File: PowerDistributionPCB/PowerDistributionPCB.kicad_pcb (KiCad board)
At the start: 4 copper layers, 89.8 x 107.2 mm, 68 parts, among them J1 USB3_A, K1 RT314F05(gen), K2 RT314F05(gen), K3 RT314F05(gen), K4 RT314F05(gen), Q1 AOD4185, Q10 MMBT2222A, Q11 MMBT2222A, Q12 MMBT2222A, Q2 MMBT2222A, Q6 MMBT2222A, Q7 MMBT2222A, Q8 MMBT2222A, Q9 MMBT2222A, U1 AP63203WU

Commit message: power traces, cleanup
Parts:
- added G***: LOGO, LOGO, F.Cu at (142.5, 62.4)
- renumbered 12V1 to 12V, 12V_OUT1 to 12V_OUT, 3.3V_OUT1 to 3.3V_OUT, 5V1 to 5V, 5V_OUT1 to 5V_OUT, 22V_BATT_IN1 to BATT_IN, J1 to VN_OUT
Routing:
- net 3.3VBuck: track 31.0 -> 212.9 mm, vias 0 -> 1
- net 5VBuck: track 25.2 -> 179.1 mm
- net 12VBuck: track 18.0 -> 128.0 mm
- net Net-(K4-Pad12.1): track 0.00 -> 7.62 mm
- net Net-(K3-Pad12.1): track 0.00 -> 7.62 mm
- net Net-(K2-Pad12.1): track 0.00 -> 7.62 mm
- net Net-(K1-Pad12.1): track 0.00 -> 7.62 mm
- net VNRelayOut: track 14.3 -> 17.2 mm
- net Sys_Vin: track 88.2 -> 86.3 mm
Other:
- board text added: "3.3V"
- board text added: "ARDUINO"
- board text added: "Power PCB SP26 Jonah Conolly Liya Mei"

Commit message: final updates to schematic and layout connections
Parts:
- added C5: 470u, Capacitor_SMD:CP_Elec_8x10.5, F.Cu at (109.5, 77.0)
- added D9: SS14, Diode_SMD:D_SMA, F.Cu at (120.5, 79.0)
- moved Cout1 4.80 mm to (98.2, 69.4)
- moved Cout2 4.80 mm to (98.2, 66.9)
- moved Cout3 4.80 mm to (98.2, 64.4)
- moved Cout4 4.80 mm to (118.4, 64.9)
- moved C2b1 4.80 mm to (100.7, 59.8)
- moved G*** 4.80 mm to (142.1, 57.6)
- moved Rfbt2 4.80 mm to (95.2, 60.4)
- moved 12V1 4.80 mm to (98.3, 60.4)
- moved C1 4.80 mm to (82.0, 60.8)
- moved C2 4.80 mm to (82.0, 66.7)
- moved Cout5 4.80 mm to (118.4, 67.4)
- moved R3a1 4.80 mm to (82.6, 57.9)
- moved R3b1 4.80 mm to (78.6, 57.9)
- moved Rfbt1 4.80 mm to (115.2, 60.9)
- moved Rmode1a1 4.80 mm to (118.5, 58.4)
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- renumbered 12V to 12V1, 12V_OUT to 12V_OUT1, BATT_IN to 22V_BATT_IN1, 3.3V_OUT to 3.3V_OUT1, 5V to 5V1, 5V_OUT to 5V_OUT1, VN_OUT to J1
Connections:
- A1 pad 27: 5VSafe -> Net-(A1-+5V)
- A1 pad 30: 12VBuck -> unconnected-(A1-VIN-Pad30)
- D10 pad 1: 5VSafe -> 5VBuck
- D2 pad 1: 5VSafe -> 5VBuck
- D3 pad 1: 5VSafe -> 5VBuck
- D4 pad 1: 5VSafe -> 5VBuck
- D5 pad 1: 5VSafe -> 5VBuck
- D6 pad 1: 5VSafe -> 5VBuck
- D7 pad 1: 5VSafe -> 5VBuck
- D8 pad 1: 5VSafe -> 5VBuck
- K1 pad 11.1: 5VBuck -> Net-(K1-Pad11.1)
- K1 pad 11.2: 5VBuck -> Net-(K1-Pad11.1)
- K1 pad 12.1: Net-(K1-Pad12.1) -> 5VBuck
- K1 pad 12.2: Net-(K1-Pad12.1) -> 5VBuck
- K1 pad A3: 5VSafe -> 5VBuck
- K2 pad 11.1: 3.3VBuck -> Net-(K2-Pad11.1)
- K2 pad 11.2: 3.3VBuck -> Net-(K2-Pad11.1)
- K2 pad 12.1: Net-(K2-Pad12.1) -> 3.3VBuck
- K2 pad 12.2: Net-(K2-Pad12.1) -> 3.3VBuck
- K2 pad A3: 5VSafe -> 5VBuck
- K3 pad 11.1: 5VBuck -> Net-(K3-Pad11.1)
- K3 pad 11.2: 5VBuck -> Net-(K3-Pad11.1)
- K3 pad 12.1: Net-(K3-Pad12.1) -> 5VBuck
- K3 pad 12.2: Net-(K3-Pad12.1) -> 5VBuck
- K3 pad A3: 5VSafe -> 5VBuck
- K4 pad 11.1: 12VBuck -> Net-(K4-Pad11.1)
- K4 pad 11.2: 12VBuck -> Net-(K4-Pad11.1)
- K4 pad 12.1: Net-(K4-Pad12.1) -> 12VBuck
- K4 pad 12.2: Net-(K4-Pad12.1) -> 12VBuck
- K4 pad A3: 5VSafe -> 5VBuck
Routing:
- net 5VSafe: track 191.7 -> 0.00 mm
- net 5VBuck: track 179.1 -> 312.5 mm, vias 0 -> 2
- net 3.3VBuck: track 212.9 -> 192.4 mm, vias 1 -> 0
- net Net-(A1-+5V): track 0.00 -> 13.3 mm
- net 12VBuck: track 128.0 -> 119.4 mm, vias 0 -> 1
- net Net-(K4-Pad12.1): track 7.62 -> 0.00 mm
- net Net-(K4-Pad11.1): track 0.00 -> 7.62 mm
- net Net-(K3-Pad12.1): track 7.62 -> 0.00 mm
- net Net-(K3-Pad11.1): track 0.00 -> 7.62 mm
- net Net-(K2-Pad12.1): track 7.62 -> 0.00 mm
- net Net-(K2-Pad11.1): track 0.00 -> 7.62 mm
- net Net-(K1-Pad12.1): track 7.62 -> 0.00 mm
- net Net-(K1-Pad11.1): track 0.00 -> 7.62 mm
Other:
- board size 89.8 x 107.2 mm -> 89.8 x 111.7 mm

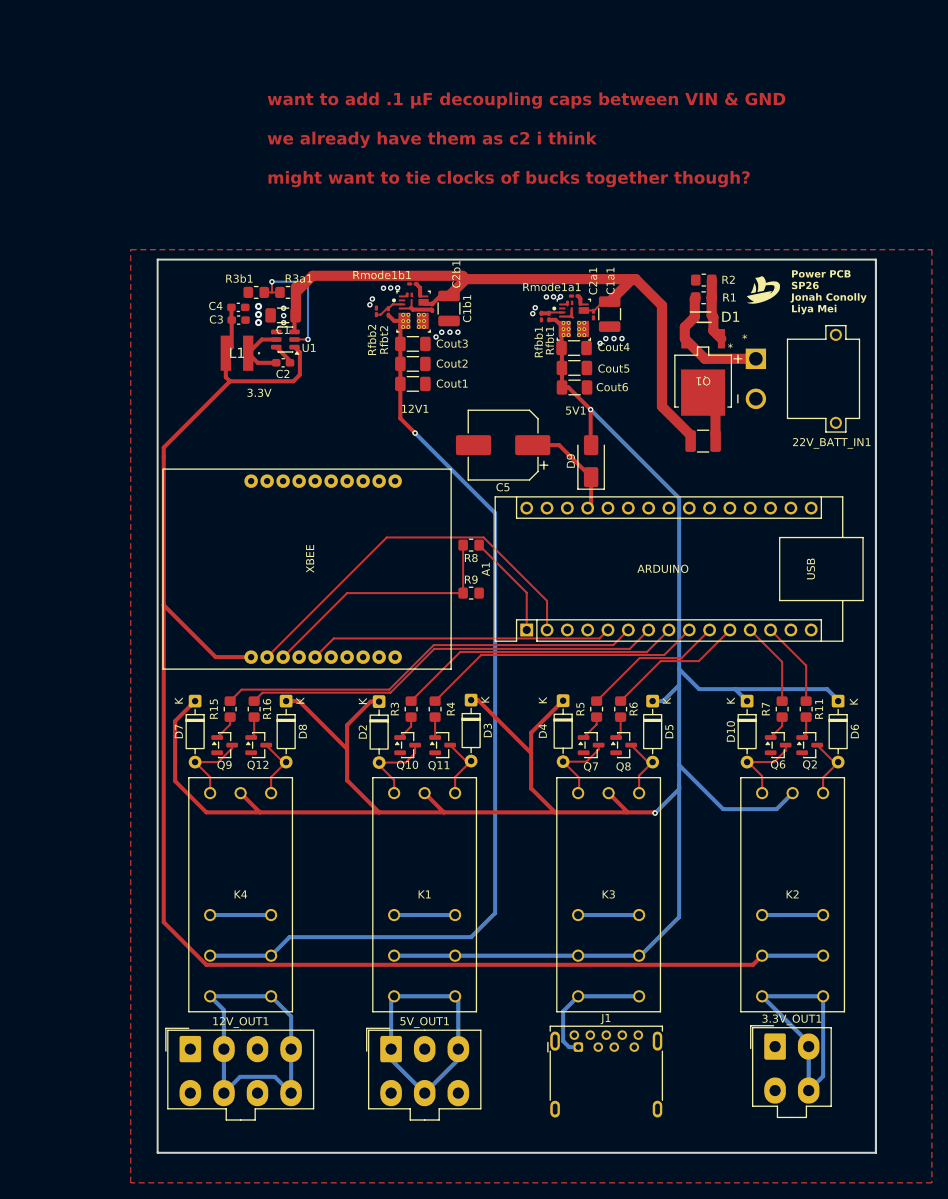
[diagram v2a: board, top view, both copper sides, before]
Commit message: updated battery protection capacitor
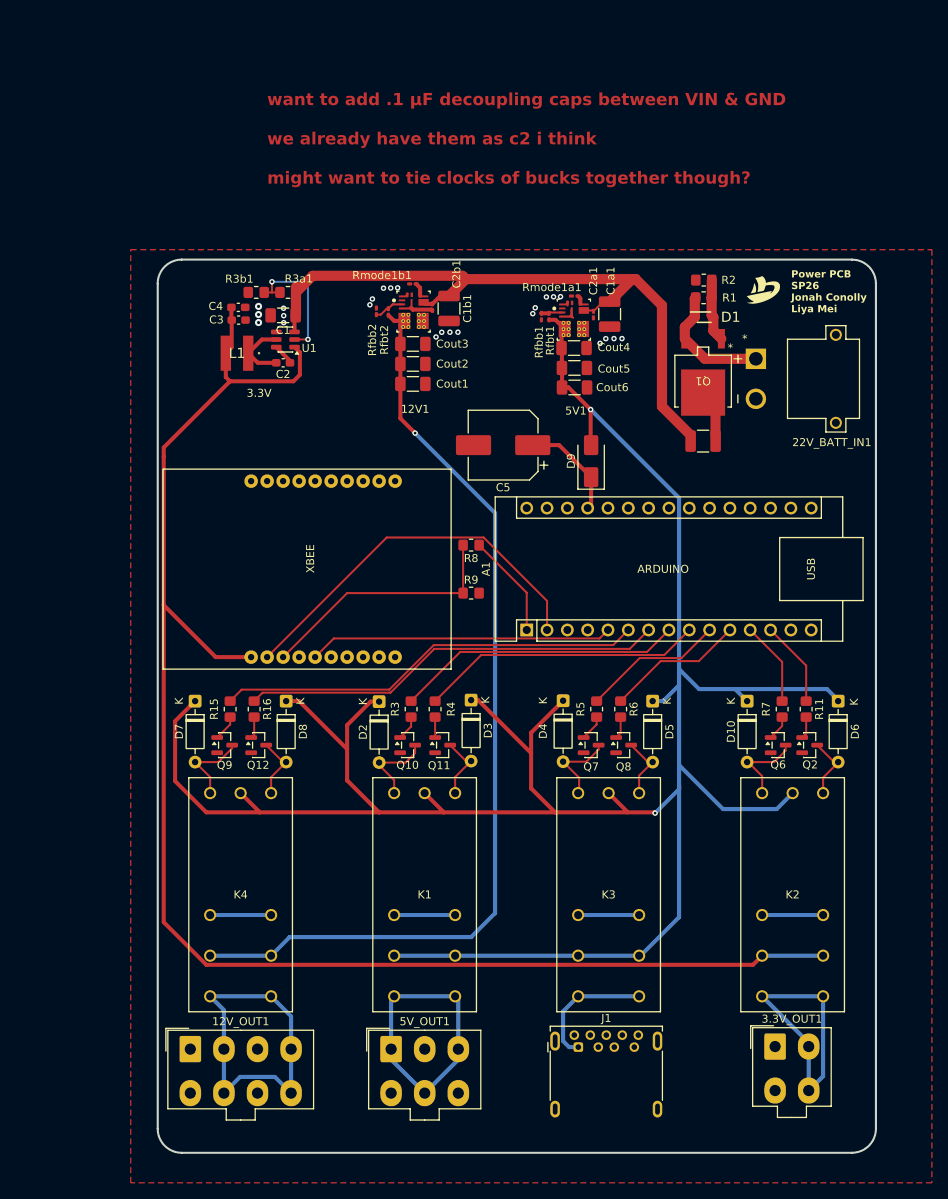
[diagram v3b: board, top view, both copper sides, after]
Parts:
- Main_Bulk(electrolytic)1: value 250µF -> 100µF
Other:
- outline, holes or cut-outs redrawn
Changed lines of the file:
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@@
 			)
 		)
-		(property "Value" "250µF"
+		(property "Value" "100µF"
 			(at 0 2.3 0)
 			(layer "F.Fab")
@@
 		)
 	)
-	(gr_rect
-		(start 66.32 53.81)
-		(end 156.1 165.46)
+	(gr_line
+		(start 153.1 165.46)
+		(end 69.32 165.46)
 		(stroke
 			(width 0.254)
-			(type solid)
+			(type default)
+		)
+		(layer "Edge.Cuts")
+	)
+	(gr_arc
+		(start 69.32 165.46)
+		(mid 67.19868 164.58132)
+		(end 66.32 162.46)
+		(stroke
+			(width 0.254)
+			(type default)
+		)
+		(layer "Edge.Cuts")
+	)
+	(gr_line
+		(start 156.1 56.81)
+		(end 156.1 162.46)
+		(stroke
+			(width 0.254)
+			(type default)
+		)
+		(layer "Edge.Cuts")
+	)
+	(gr_arc
+		(start 156.1 162.46)
+		(mid 155.22132 164.58132)
+		(end 153.1 165.46)
+		(stroke
+			(width 0.254)
+			(type default)
+		)
+		(layer "Edge.Cuts")
+	)
+	(gr_line
+		(start 69.32 53.81)
+		(end 153.1 53.81)
+		(stroke
+			(width 0.254)
+			(type default)
+		)
+		(layer "Edge.Cuts")
+	)
+	(gr_arc
+		(start 153.1 53.81)
+		(mid 155.22132 54.68868)
+		(end 156.1 56.81)
+		(stroke
+			(width 0.254)
+			(type default)
+		)
+		(layer "Edge.Cuts")
+	)
+	(gr_line
+		(start 66.32 162.46)
+		(end 66.32 56.81)
+		(stroke
+			(width 0.254)
+			(type default)
+		)
+		(layer "Edge.Cuts")
+	)
+	(gr_arc
+		(start 66.32 56.81)
+		(mid 67.19868 54.68868)
+		(end 69.32 53.81)
+		(stroke
+			(width 0.254)
+			(type default)
 		)
-		(fill no)
 		(layer "Edge.Cuts")
 	)

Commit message: fixed DRC errors
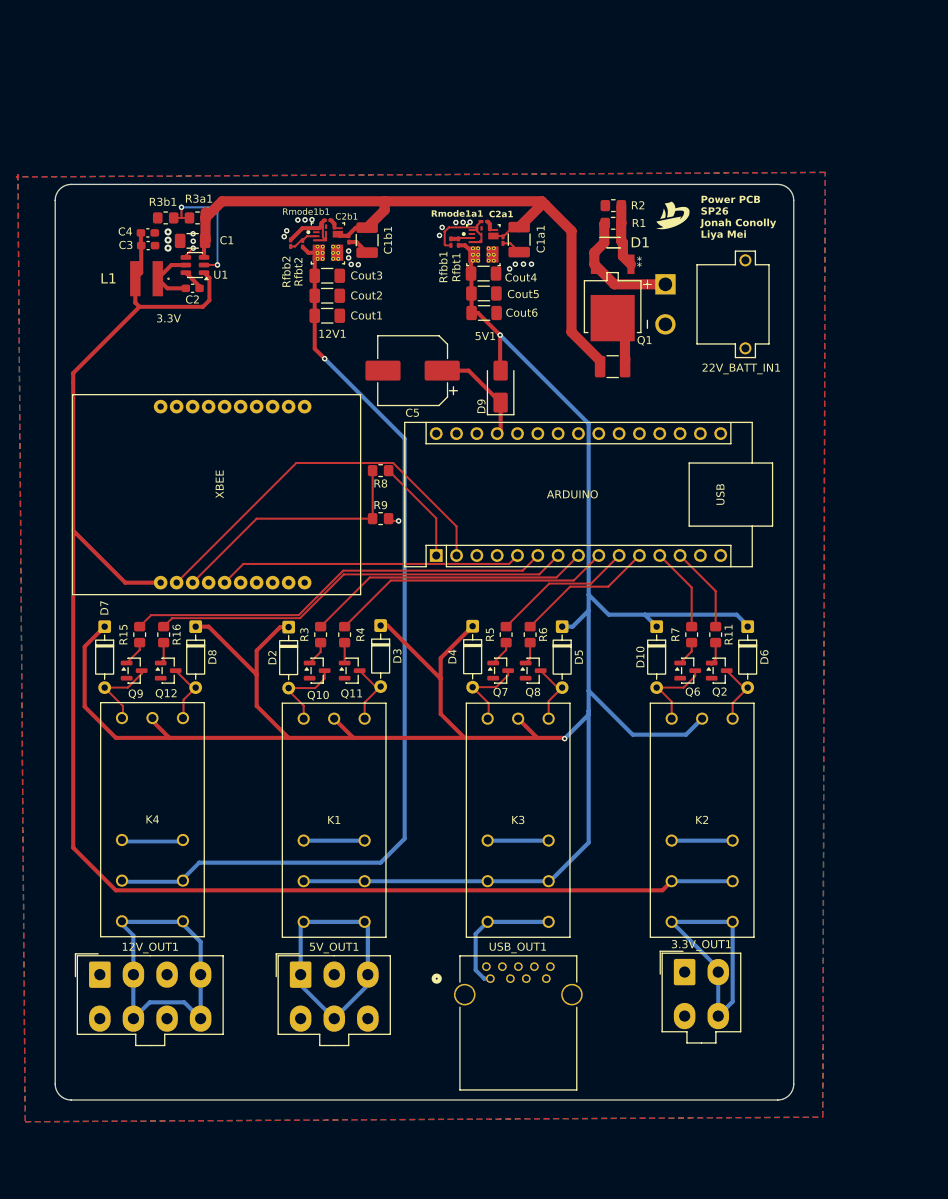
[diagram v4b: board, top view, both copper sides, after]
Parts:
- removed J1: USB3_A, Connector_USB:USB3_A_Molex_48393-001
- added USB_OUT1: 484050003, CUSail:CONN_484050003_MOL, F.Cu at (107.9, 143.7)
- moved R2 14.6 mm to (123.3, 47.1)
- moved 12V_OUT1 14.6 mm to (59.1, 143.2)
- moved 22V_BATT_IN1 14.6 mm to (139.8, 59.4)
- moved 3.3V_OUT1 14.6 mm to (132.2, 142.9)
- moved 5V1 14.6 mm to (107.0, 52.1)
- moved 5V_OUT1 14.6 mm to (84.2, 143.2)
- moved A1 14.6 mm to (101.1, 90.8)
- moved C2a1 14.6 mm to (109.5, 51.4)
- moved C3 14.6 mm to (65.1, 52.1)
- moved C4 14.6 mm to (65.1, 50.5)
- moved C5 14.6 mm to (98.2, 67.7)
- moved Cout6 14.6 mm to (107.1, 60.5)
- moved D10 14.6 mm to (128.7, 99.7)
- moved D2 14.6 mm to (82.7, 99.8)
- moved D3 14.6 mm to (94.2, 99.6)
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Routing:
- net GND: track 5.63 -> 42.3 mm, vias 6 -> 7
- net Sys_Vin: track 86.3 -> 87.5 mm
- net 12VBuck: track 119.4 -> 118.4 mm
- net Net-(12V1-MODE): track 1.70 -> 1.18 mm
- added copper zone on B.Cu, net GND
- added copper zone on In1.Cu, net GND
- added copper zone on In2.Cu, net GND
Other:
- board size 89.8 x 111.7 mm -> 92.3 x 114.5 mm
- board text removed: "want to add .1 µF decoupling caps between VIN & GND we already have them as c2 i think might want to tie clocks of bucks together though?"

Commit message: added clipart
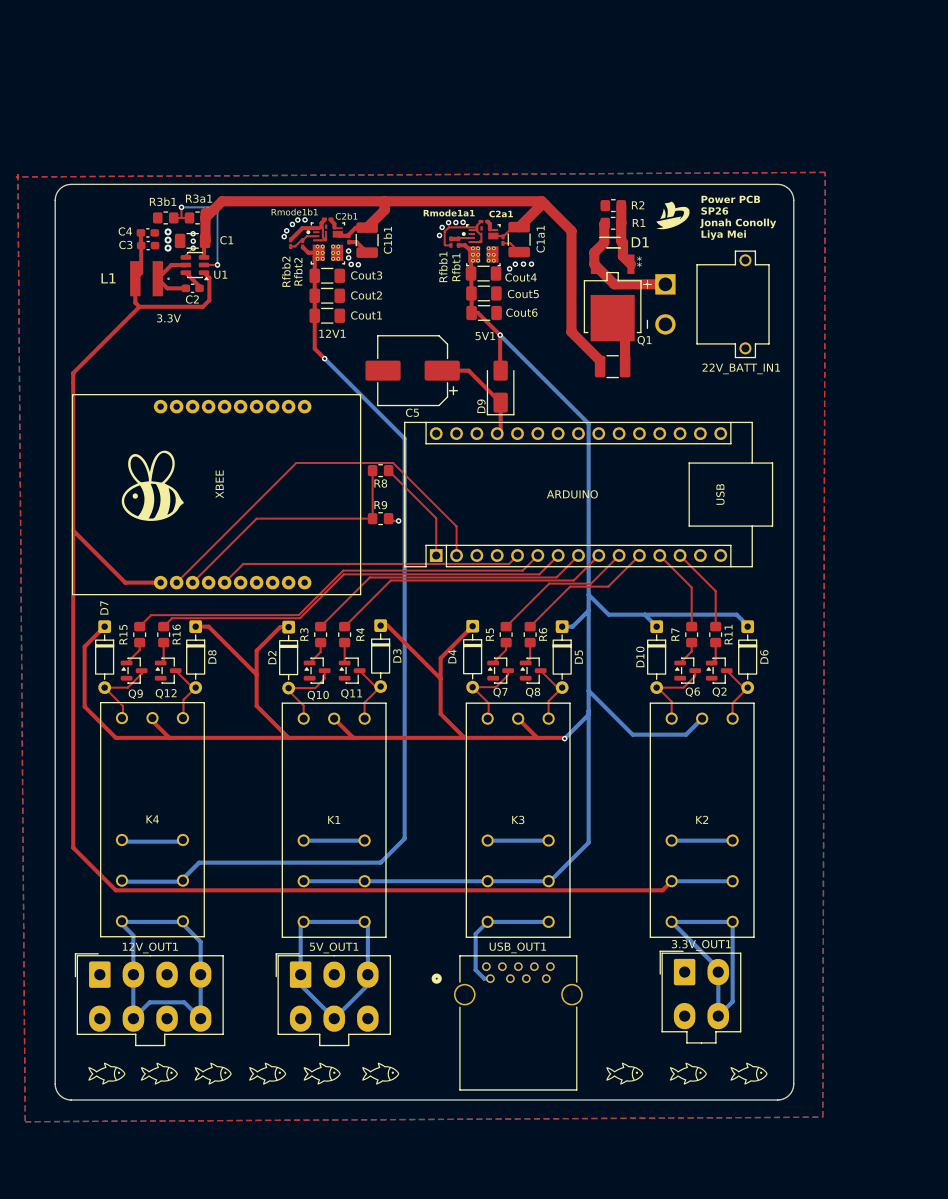
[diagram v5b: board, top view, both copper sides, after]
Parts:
- added G***: LOGO, LOGO, F.Cu at (124.7, 155.6)
- added G***: LOGO, LOGO, F.Cu at (66.5, 155.6)
- added G***: LOGO, LOGO, F.Cu at (132.7, 155.6)
- added G***: LOGO, LOGO, F.Cu at (60.0, 155.6)
- added G***: LOGO, LOGO, F.Cu at (65.8, 82.2)
- added G***: LOGO, LOGO, F.Cu at (94.2, 155.6)
- added G***: LOGO, LOGO, F.Cu at (86.9, 155.6)
- added G***: LOGO, LOGO, F.Cu at (80.1, 155.6)
- added G***: LOGO, LOGO, F.Cu at (140.2, 155.6)
- added G***: LOGO, LOGO, F.Cu at (73.3, 155.6)
- moved Rmode1b1 0.15 mm to (87.6, 48.8)
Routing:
- net GND: track 42.3 -> 41.6 mm

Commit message: new buck stuff
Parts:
- removed C1a1: 10uF, Capacitor_SMD:C_1210_3225Metric_Pad1.33x2.70mm_HandSolder
- removed C2a1: 100nF, Capacitor_SMD:C_0201_0603Metric_Pad0.64x0.40mm_HandSolder
- removed Cout4, Cout5, Cout6: 22uF, Capacitor_SMD:C_1206_3216Metric_Pad1.33x1.80mm_HandSolder
- added Cboot1: 100nF, Capacitor_SMD:C_0201_0603Metric_Pad0.64x0.40mm_HandSolder, F.Cu at (95.4, 45.1)
- added Cff1: 150pF, Capacitor_SMD:C_0201_0603Metric_Pad0.64x0.40mm_HandSolder, F.Cu at (94.0, 52.5)
- added Cin1: 10µF, Capacitor_SMD:C_1210_3225Metric_Pad1.33x2.70mm_HandSolder, F.Cu at (82.4, 46.9)
- added Cin2: 10µF, Capacitor_SMD:C_1210_3225Metric_Pad1.33x2.70mm_HandSolder, F.Cu at (86.4, 46.9)
- added Cinx1: 100nF, Capacitor_SMD:C_0805_2012Metric_Pad1.18x1.45mm_HandSolder, F.Cu at (89.9, 47.0)
- added Cout1a1: 22µF, Capacitor_SMD:C_1210_3225Metric_Pad1.33x2.70mm_HandSolder, F.Cu at (106.9, 48.9)
- added Cout2a1: 22µF, Capacitor_SMD:C_1210_3225Metric_Pad1.33x2.70mm_HandSolder, F.Cu at (110.9, 48.9)
- added Css1: 22nF, Capacitor_SMD:C_0402_1005Metric_Pad0.74x0.62mm_HandSolder, F.Cu at (97.9, 51.4)
- added L1a1: 3.3µH, Inductor_SMD:L_Coilcraft_XAL7070-XXX, F.Cu at (100.5, 45.0)
- added Rpg1: 100kΩ, Resistor_SMD:R_0402_1005Metric_Pad0.72x0.64mm_HandSolder, F.Cu at (96.4, 51.1)
- 5V1: value TPSM84338RCJR -> TPS56A37RPAR; footprint CUSail:buck_correct -> CUSail:TPS56A37RPAR
- Rfbb1: value 10k -> 10kΩ
- Rfbt1: value 73.2k -> 73.2kΩ; footprint Resistor_SMD:R_0201_0603Metric_Pad0.64x0.40mm_HandSolder -> Resistor_SMD:R_0805_2012Metric_Pad1.20x1.40mm_HandSolder
- Rmode1a1: value 18k -> 52.3kΩ; footprint Capacitor_SMD:C_0201_0603Metric_Pad0.64x0.40mm_HandSolder -> Resistor_SMD:R_0402_1005Metric_Pad0.72x0.64mm_HandSolder
- moved Rmode1a1 15.4 mm to (91.9, 51.4), turned to -90 degrees
- moved 5V1 13.6 mm to (94.1, 47.9), turned to 90 degrees
- moved C1b1 13.1 mm to (81.0, 57.5)
- moved Cout1b1 13.1 mm to (76.0, 67.0)
- moved Cout2b1 13.1 mm to (76.0, 64.5)
- moved Cout3b1 13.1 mm to (76.0, 62.0)
- moved Rfbt2 13.1 mm to (72.9, 58.0)
- moved Rmode1b1 13.1 mm to (76.1, 54.9)
- moved 12V1 13.1 mm to (76.1, 58.0)
- moved Rfbb2 13.1 mm to (71.4, 57.9)
- moved C2b1 13.1 mm to (78.7, 57.4)
- moved Rfbt1 11.0 mm to (93.4, 55.0)
- moved Rfbb1 9.02 mm to (94.0, 51.0), turned to 0 degrees
- moved C3 7.25 mm to (58.2, 50.1)
- moved L1b1 7.25 mm to (58.0, 54.2)
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- renumbered Cout1 to Cout1b1, Cout2 to Cout2b1, Cout3 to Cout3b1, L1 to L1b1, USB_OUT1 to USB_Connect1
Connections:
- 5V1 pad 4: 5VBuck -> Net-(5V1-PG)
- 5V1 pad 5: unconnected-(5V1-SW-Pad5)_2 -> Net-(5V1-SS)
- 5V1 pad 6: Sys_Vin -> Net-(5V1-SW)
- 5V1 pad 7: Net-(5V1-MODE) -> Net-(5V1-BOOT)
- 5V1 pad 8: unconnected-(5V1-SS_PG-Pad8) -> Sys_Vin
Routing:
- net Sys_Vin: track 87.5 -> 112.0 mm
- net 5VBuck: track 312.5 -> 297.9 mm
- net GND: track 41.6 -> 29.2 mm
- net 12VBuck: track 118.4 -> 125.0 mm
- net Net-(5V1-FB): track 2.90 -> 0.00 mm
- net Net-(5V1-MODE): track 1.12 -> 0.00 mm
- net 3.3VBuck: track 192.4 -> 191.5 mm
- net (no net): vias 18 -> 9
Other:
- board size 92.3 x 114.5 mm -> 92.3 x 122.5 mm
